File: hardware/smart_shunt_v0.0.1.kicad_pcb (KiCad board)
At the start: 2 copper layers, 63.8 x 34.3 mm, 48 parts, among them J1 SHUNT +, J2 SHUNT -, J3 VIn, J4 USB_C_Receptacle_USB2.0, J5 GND, SW1 SW_Push, SW2 SW_Push, U1 ESP32-C3-MINI-1, U4 INA226, U5 TPS562201

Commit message: v0.0.2 update, before FETs
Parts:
- removed JP1 (x2): SolderJumper_2_Open, Jumper:SolderJumper-2_P1.3mm_Open_TrianglePad1.0x1.5mm
- removed TP3, TP4 (x4), TP5, TP6, TP7, TP8, TP9: TestPoint, TestPoint:TestPoint_Pad_D1.0mm
- added D5: 1N5819WS, Diode_SMD:D_SOD-323, F.Cu at (136.9, 92.2)
- J1, J2: footprint Acea:MountingHole_10.5mm -> ShuntToPCB:MountingHole_17mm
- moved SW2 54.1 mm to (167.3, 68.9), turned to 0 degrees
- moved SW1 52.1 mm to (119.9, 68.9), turned to 0 degrees
- moved J1 48.6 mm to (167.4, 81.7), turned to 180 degrees
- moved J2 46.4 mm to (119.9, 81.7), turned to 180 degrees
- moved J5 38.0 mm to (154.5, 96.0), turned to 180 degrees
- moved J3 36.7 mm to (132.7, 96.0), turned to 180 degrees
- moved J4 34.3 mm to (143.7, 98.0), turned to 0 degrees
- moved C8 31.2 mm to (130.2, 89.0), turned to 90 degrees
- moved C5 26.9 mm to (135.9, 69.5), turned to 90 degrees
- moved R10 24.6 mm to (147.2, 92.4), turned to 180 degrees
- moved R9 23.8 mm to (140.2, 92.4), turned to 0 degrees
- moved G*** 23.3 mm to (154.3, 83.8), turned to 0 degrees
- moved D1 23.3 mm to (143.6, 92.5), turned to 180 degrees
- moved U4 22.8 mm to (134.6, 88.5), turned to 180 degrees
- moved R6 21.8 mm to (135.9, 72.6), turned to -90 degrees
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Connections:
- C4 pad 1: BATTV -> SHUNT+
- C6 pad 1: BATTV -> SHUNT+
- J3 pad 1: BATTV -> unconnected-(J3-Pin_1-Pad1)
- U1 pad 19: unconnected-(U1-GPIO5/ADC2_CH0-Pad19) -> LOAD_DISCONNECT
- U4 pad 8: BATTV -> SHUNT+
- U5 pad 3: BATTV -> SHUNT+
- U5 pad 5: BATTV -> SHUNT+
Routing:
- net BATTV: track 24.6 -> 0.00 mm, vias 1 -> 0
- net GND: track 72.5 -> 61.8 mm
- net SHUNT-: track 16.0 -> 9.38 mm
- net USB_VBUS: track 6.52 -> 12.1 mm
- net Net-(U1-EN/CHIP_PU): track 32.9 -> 27.4 mm
- net Net-(U1-GPIO9): track 38.6 -> 33.2 mm
- net SHUNT+: track 50.5 -> 54.0 mm, vias 2 -> 0
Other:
- board size 63.8 x 34.3 mm -> 66.1 x 34.3 mm
- board text added: "AE-SMART-SHUNT Hi-side Shunt v0.0.2"
- board text added: "AUX BATT-"
- board text added: "CAR BATT+"
- board text added: "TO AUX BATT +"
- board text added: "TO LOAD +"
- board text removed: "3.3"
- board text removed: "AE-SMART-SHUNT v0.0.1 bi-directional hi/low side"
- board text removed: "B"
- board text removed: "BATT+"
- board text removed: "BATT-"
- board text removed: "G"
- board text removed: "GND"
- board text removed: "R"
- board text removed: "S+"
- board text removed: "S-"
- board text removed: "TO BATT"
- board text removed: "TO LOAD"

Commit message: v0.0.3 off to JLCPCB
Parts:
- added C11: 100nF, Capacitor_SMD:C_0603_1608Metric, F.Cu at (178.8, 98.9)
- added C12: 220nF, Capacitor_SMD:C_0805_2012Metric, F.Cu at (175.8, 99.1)
- added C13: 220uF 50V, Capacitor_SMD:CP_Elec_8x10.5, F.Cu at (165.4, 96.2)
- added J6: SHUNT +, ShuntToPCB:MountingHole_17mm, F.Cu at (201.0, 79.4)
- added Q1: CMSL008N06, CMSL008N06:CMSL008N06, F.Cu at (184.4, 73.2)
- added Q2: CMSL008N06, CMSL008N06:CMSL008N06, F.Cu at (184.4, 84.8)
- added R13: 33.2k, Resistor_SMD:R_0603_1608Metric, F.Cu at (130.0, 91.1)
- added R14: 180k, Resistor_SMD:R_0603_1608Metric, F.Cu at (133.2, 91.1)
- added U2: LM74502H-Q1, Package_TO_SOT_SMD:SOT-23-8, F.Cu at (175.8, 96.1)
- moved C8 0.26 mm to (130.2, 88.8)
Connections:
- J3 pad 1: unconnected-(J3-Pin_1-Pad1) -> Net-(J3-Pin_1)
- U1 pad 19: LOAD_DISCONNECT -> LD_DISC
- U1 pad 6: unconnected-(U1-GPIO3/ADC1_CH3-Pad6) -> Net-(U1-GPIO3/ADC1_CH3)
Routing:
- net LD_DISC: track 0.00 -> 49.9 mm, vias 0 -> 2
- net GATE: track 0.00 -> 33.6 mm
- net Net-(U1-GPIO3/ADC1_CH3): track 0.00 -> 26.1 mm, vias 0 -> 4
- net Net-(J6-Pin_1): track 0.00 -> 17.6 mm, vias 0 -> 128
- net GND: track 61.8 -> 69.7 mm, vias 39 -> 41
- net SHUNT+: track 54.0 -> 59.0 mm, vias 0 -> 236
- net Net-(J3-Pin_1): track 0.00 -> 3.04 mm
- net VCAP: track 0.00 -> 2.10 mm
- added copper zone on B.Cu, net Net-(J6-Pin_1)
- added copper zone on F.Cu, net Net-(J6-Pin_1)
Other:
- board size 66.1 x 34.3 mm -> 99.7 x 34.3 mm
- board text added: "AE-SMART-SHUNT v0.0.3"
- board text removed: "AE-SMART-SHUNT v0.0.1"
- board text removed: "GND BRIDGE"

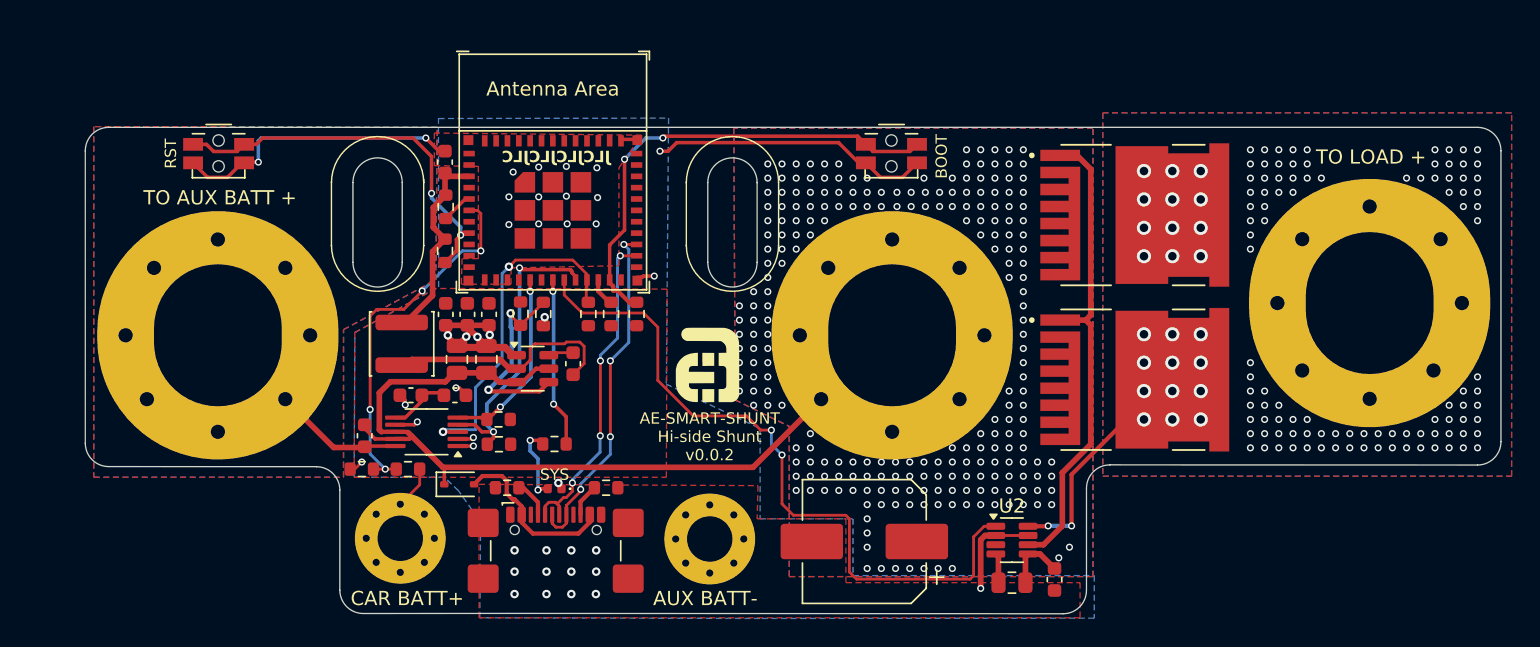
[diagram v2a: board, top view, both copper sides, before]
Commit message: Fixing reversed MOSFETs
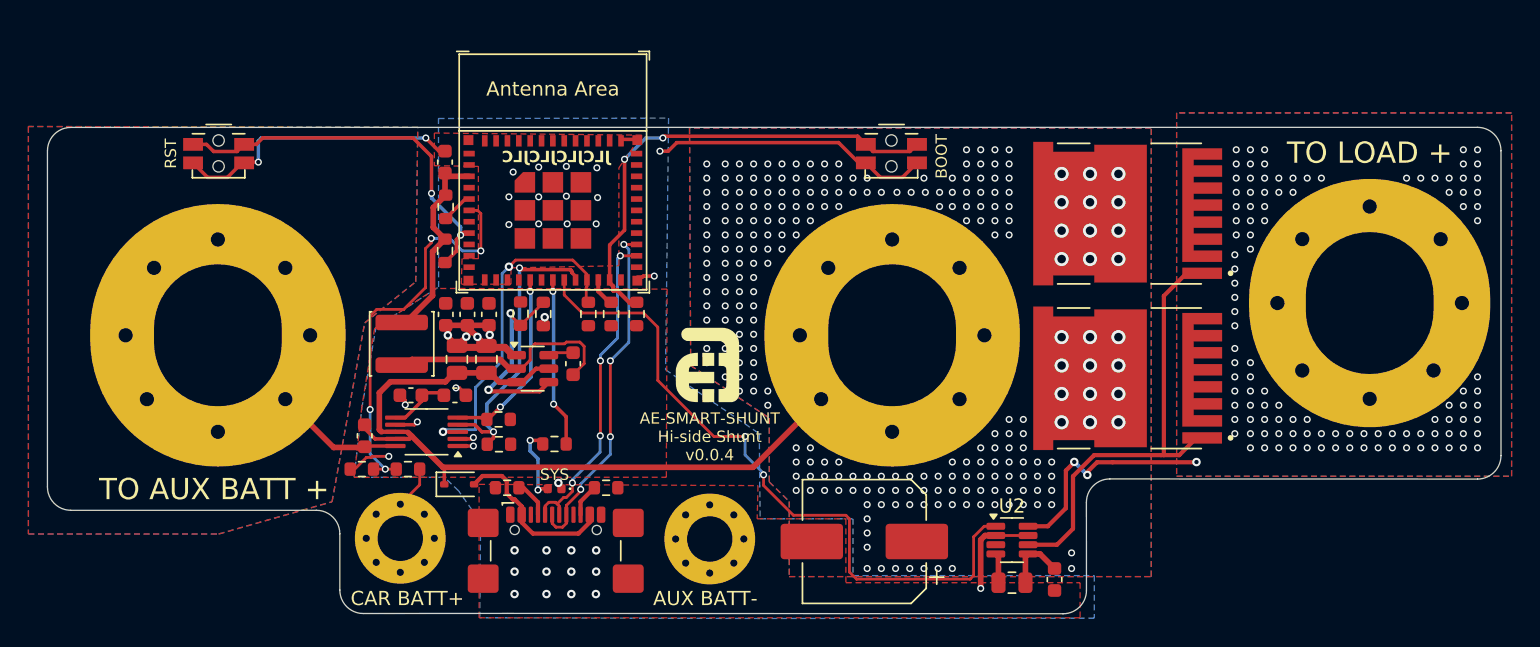
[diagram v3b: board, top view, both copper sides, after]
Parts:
- J6: value SHUNT + -> Load Out
- moved Q2 11.7 mm to (183.9, 73.1), turned to 180 degrees
- moved Q1 11.5 mm to (183.9, 84.7), turned to 180 degrees
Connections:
- Q1 pad 2: SHUNT+ -> Net-(J6-Pin_1)
- Q1 pad 3: Net-(J6-Pin_1) -> SHUNT+
- Q2 pad 2: SHUNT+ -> Net-(J6-Pin_1)
- Q2 pad 3: Net-(J6-Pin_1) -> SHUNT+
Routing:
- net Net-(U1-GPIO3/ADC1_CH3): track 26.1 -> 28.6 mm
- net GND: track 69.7 -> 71.8 mm
- net GATE: track 33.6 -> 32.1 mm
- net Net-(J6-Pin_1): track 17.6 -> 16.2 mm, vias 128 -> 115
- net SHUNT+: track 59.0 -> 60.4 mm, vias 236 -> 252
- net LD_DISC: track 49.9 -> 48.8 mm
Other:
- board size 99.7 x 34.3 mm -> 102.4 x 34.3 mm
- board text added: "AE-SMART-SHUNT Hi-side Shunt v0.0.4"
- board text added: "AE-SMART-SHUNT v0.0.4"
- board text removed: "AE-SMART-SHUNT Hi-side Shunt v0.0.2"
- board text removed: "AE-SMART-SHUNT v0.0.3"

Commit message: Fixing ADC trace - Thanks Vincent!
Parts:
- moved C7 0.54 mm to (145.4, 83.5)
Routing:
- net SHUNT+: track 60.4 -> 64.6 mm, vias 252 -> 254
- net LD_DISC: track 48.8 -> 47.6 mm
- net Net-(U5-SW): track 16.3 -> 17.2 mm
